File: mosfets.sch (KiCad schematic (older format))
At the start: 53 parts, among them J11 Conn_01x02, J12 Conn_01x02, J13 Conn_01x02, J14 Conn_01x02, J17 Conn_01x02, J18 Conn_01x02, J19 Conn_01x02, J20 Conn_01x02, J44 Conn_01x02, J45 Conn_01x02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

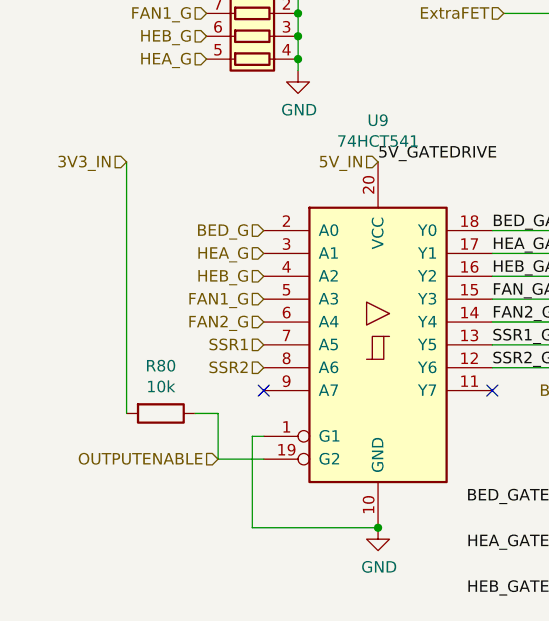
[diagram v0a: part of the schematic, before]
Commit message: Deglitch 5V level shifter for FET gate drive: - pullups on the SSR inputs - pullup to 5V on enable pin - ground channel 8
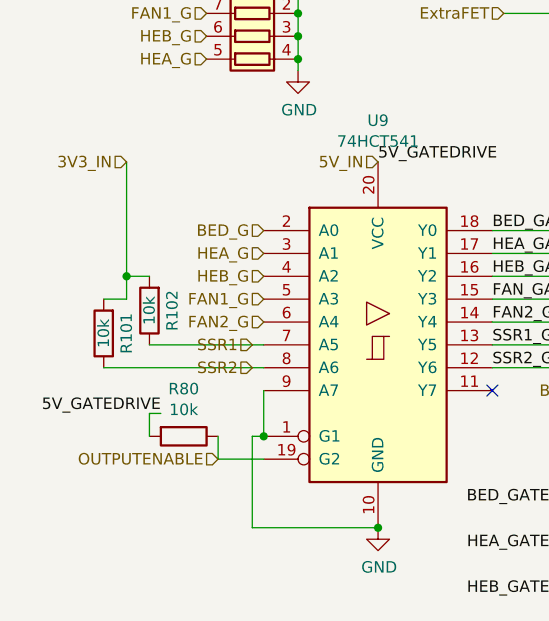
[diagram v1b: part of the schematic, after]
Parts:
- added R101, R102: 10k, Resistor_SMD:R_0402_1005Metric, symbol Device:R
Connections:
- net 3V3_IN: now also R101.2, R102.2; no longer R80.2
- net 5V_IN: now also R80.2
- net GND: now also U9.9 (A7)
- net SSR1: now also R102.1
- net SSR2: now also R101.1
- no-connect marks 2 -> 1
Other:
- moved on the sheet: R80
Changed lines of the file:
@@
 $Descr A4 11693 8268
 encoding utf-8
-Sheet 3 10
+Sheet 7 10
 Title ""
 Date ""
@@
 Text HLabel 850  4700 0    50   Input ~ 0
 3V3_IN
-Text HLabel 1450 5500 0    50   Input ~ 0
+Text HLabel 1400 5500 0    50   Input ~ 0
 SSR1
-Text HLabel 1450 5600 0    50   Input ~ 0
+Text HLabel 1400 5600 0    50   Input ~ 0
 SSR2
 Text HLabel 2500 4050 0    50   Input ~ 0
@@
 OUTPUTENABLE
 Wire Wire Line
-	850  4700 850  5800
+	850  4700 850  5200
 $Comp
 L Device:R R80
 U 1 1 63B15BCF
-P 1000 5800
-F 0 "R80" V 793 5800 50  0000 C CNN
-F 1 "10k" V 884 5800 50  0000 C CNN
-F 2 "Resistor_SMD:R_0402_1005Metric" V 930 5800 50  0001 C CNN
-F 3 "~" H 1000 5800 50  0001 C CNN
-	1    1000 5800
-	0    1    1    0
-$EndComp
-Wire Wire Line
-	1150 5800 1250 5800
+P 1100 5900
+F 0 "R80" V 893 5900 50  0000 C CNN
+F 1 "10k" V 984 5900 50  0000 C CNN
+F 2 "Resistor_SMD:R_0402_1005Metric" V 1030 5900 50  0001 C CNN
+F 3 "~" H 1100 5900 50  0001 C CNN
+	1    1100 5900
+	0    1    1    0
+$EndComp
 Wire Wire Line
 	3350 5100 3350 5000
@@
 Wire Wire Line
 	2950 5000 2450 5000
-Wire Wire Line
-	1250 5800 1250 6000
 Wire Wire Line
 	1250 6000 1450 6000
@@
 Wire Wire Line
 	3000 2200 2900 2200
-NoConn ~ 1450 5700
 Wire Wire Line
 	4250 2100 4250 1200
@@
 Text HLabel 1200 4250 0    50   Input ~ 0
 HEA_G
+$Comp
+L Device:R R102
+U 1 1 6264E949
+P 950 5350
+F 0 "R102" V 850 5350 50  0000 C CNN
+F 1 "10k" V 950 5350 50  0000 C CNN
+F 2 "Resistor_SMD:R_0402_1005Metric" V 880 5350 50  0001 C CNN
+F 3 "~" H 950 5350 50  0001 C CNN
+	1    950  5350
+	-1   0    0    1
+$EndComp
+$Comp
+L Device:R R101
+U 1 1 6265222C
+P 750 5450
+F 0 "R101" V 650 5450 50  0000 C CNN
+F 1 "10k" V 750 5450 50  0000 C CNN
+F 2 "Resistor_SMD:R_0402_1005Metric" V 680 5450 50  0001 C CNN
+F 3 "~" H 750 5450 50  0001 C CNN
+	1    750  5450
+	-1   0    0    1
+$EndComp
+Wire Wire Line
+	950  5200 850  5200
+Connection ~ 850  5200
+Wire Wire Line
+	850  5200 850  5300
+Wire Wire Line
+	750  5300 850  5300
+Wire Wire Line
+	1450 5500 950  5500
+Wire Wire Line
+	1450 5600 750  5600
+Wire Wire Line
+	1450 5700 1450 5900
+Connection ~ 1450 5900
+Text Label 1000 5800 2    50   ~ 0
+5V_GATEDRIVE
+Wire Wire Line
+	1250 5900 1250 6000
+Wire Wire Line
+	1000 5800 950  5800
+Wire Wire Line
+	950  5800 950  5900
 $EndSCHEMATC

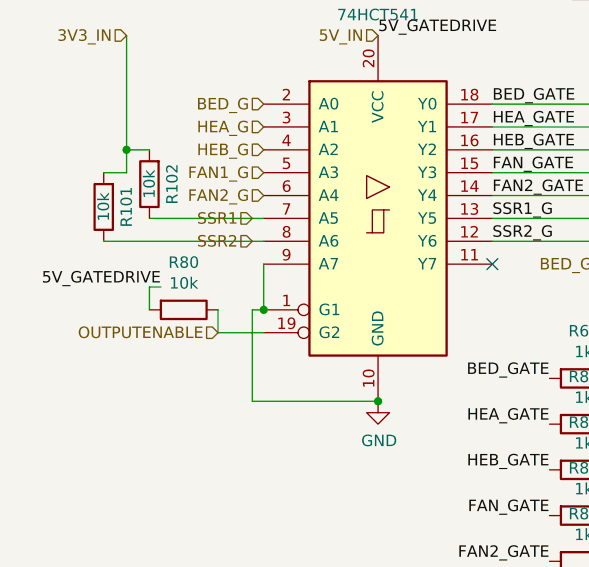
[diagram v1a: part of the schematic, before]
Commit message: Move board thermistor, move LED resistors, add diode to probe input, NC header on probe input, change pullup on probe input, change value of enable resistor for fet driver, add ideal diode to schmatic, add fiducials to board, swap T1 and T4 opamp output
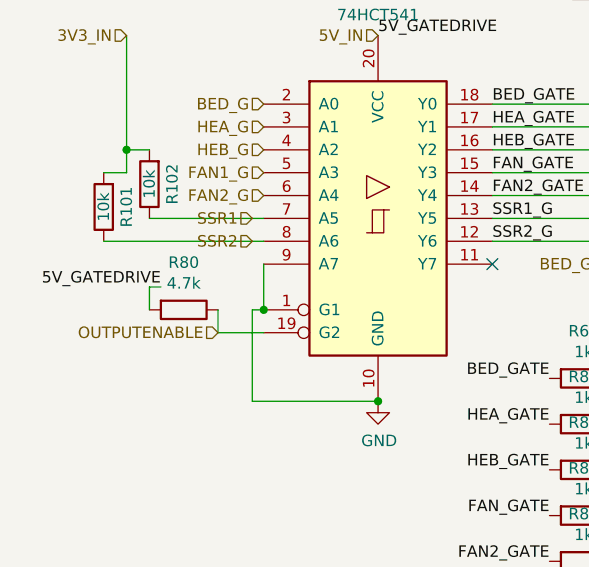
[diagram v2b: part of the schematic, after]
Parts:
- R80: value 10k -> 4.7k
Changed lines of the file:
@@
 $Descr A4 11693 8268
 encoding utf-8
-Sheet 7 10
+Sheet 7 13
 Title ""
 Date ""
@@
 P 1100 5900
 F 0 "R80" V 893 5900 50  0000 C CNN
-F 1 "10k" V 984 5900 50  0000 C CNN
+F 1 "4.7k" V 984 5900 50  0000 C CNN
 F 2 "Resistor_SMD:R_0402_1005Metric" V 1030 5900 50  0001 C CNN
 F 3 "~" H 1100 5900 50  0001 C CNN

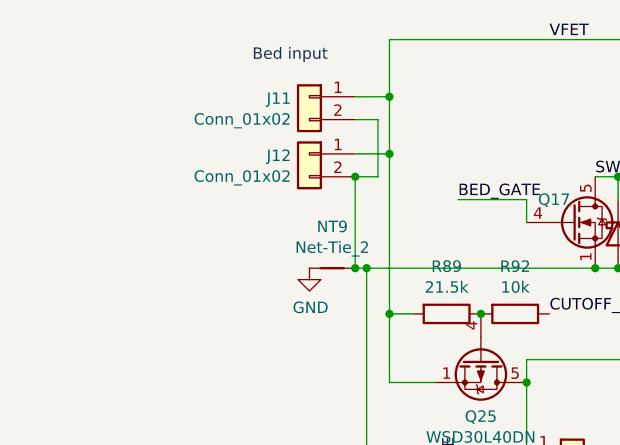
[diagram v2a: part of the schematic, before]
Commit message: Adapt 2590 board layout to ideal diodes and dual power input connector
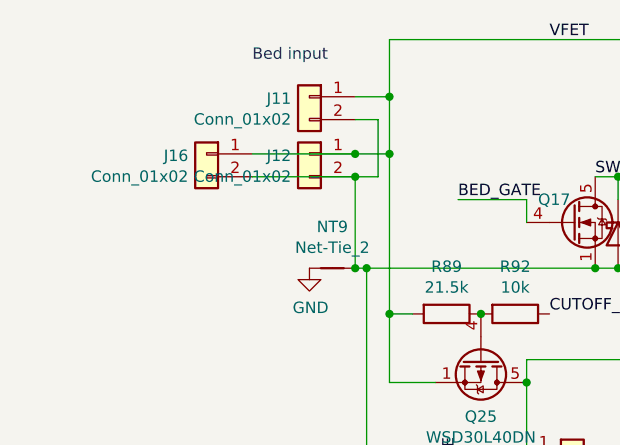
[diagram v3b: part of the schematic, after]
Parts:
- added J16: Conn_01x02, smoothieparts:XT30, symbol Connector_Generic:Conn_01x02
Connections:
- net GND_FET: now also J16.2 (Pin_2)
- net VFET: now also J16.1 (Pin_1)
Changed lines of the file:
@@
 $Descr A4 11693 8268
 encoding utf-8
-Sheet 7 13
+Sheet 3 13
 Title ""
 Date ""
@@
 Wire Wire Line
 	950  5800 950  5900
+$Comp
+L Connector_Generic:Conn_01x02 J?
+U 1 1 63AE783B
+P 1200 1700
+AR Path="/63AE783B" Ref="J?"  Part="1"
+AR Path="/612538A5/63AE783B" Ref="J16"  Part="1"
+F 0 "J16" H 1280 1692 50  0000 L CNN
+F 1 "Conn_01x02" H 1280 1601 50  0000 L CNN
+F 2 "smoothieparts:XT30" H 1200 1700 50  0001 C CNN
+F 3 "~" H 1200 1700 50  0001 C CNN
+	1    1200 1700
+	-1   0    0    -1
+$EndComp
+Wire Wire Line
+	1400 1700 1850 1700
+Connection ~ 1850 1700
+Wire Wire Line
+	1400 1800 1850 1800
 $EndSCHEMATC
